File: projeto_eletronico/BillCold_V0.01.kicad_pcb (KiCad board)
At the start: 2 copper layers, 36 parts, among them J1 USB_B, U1 ESP32-S3, U2 AMS1117, U3 W25Q128JVSIQ, X1 OSCILADOR-3225

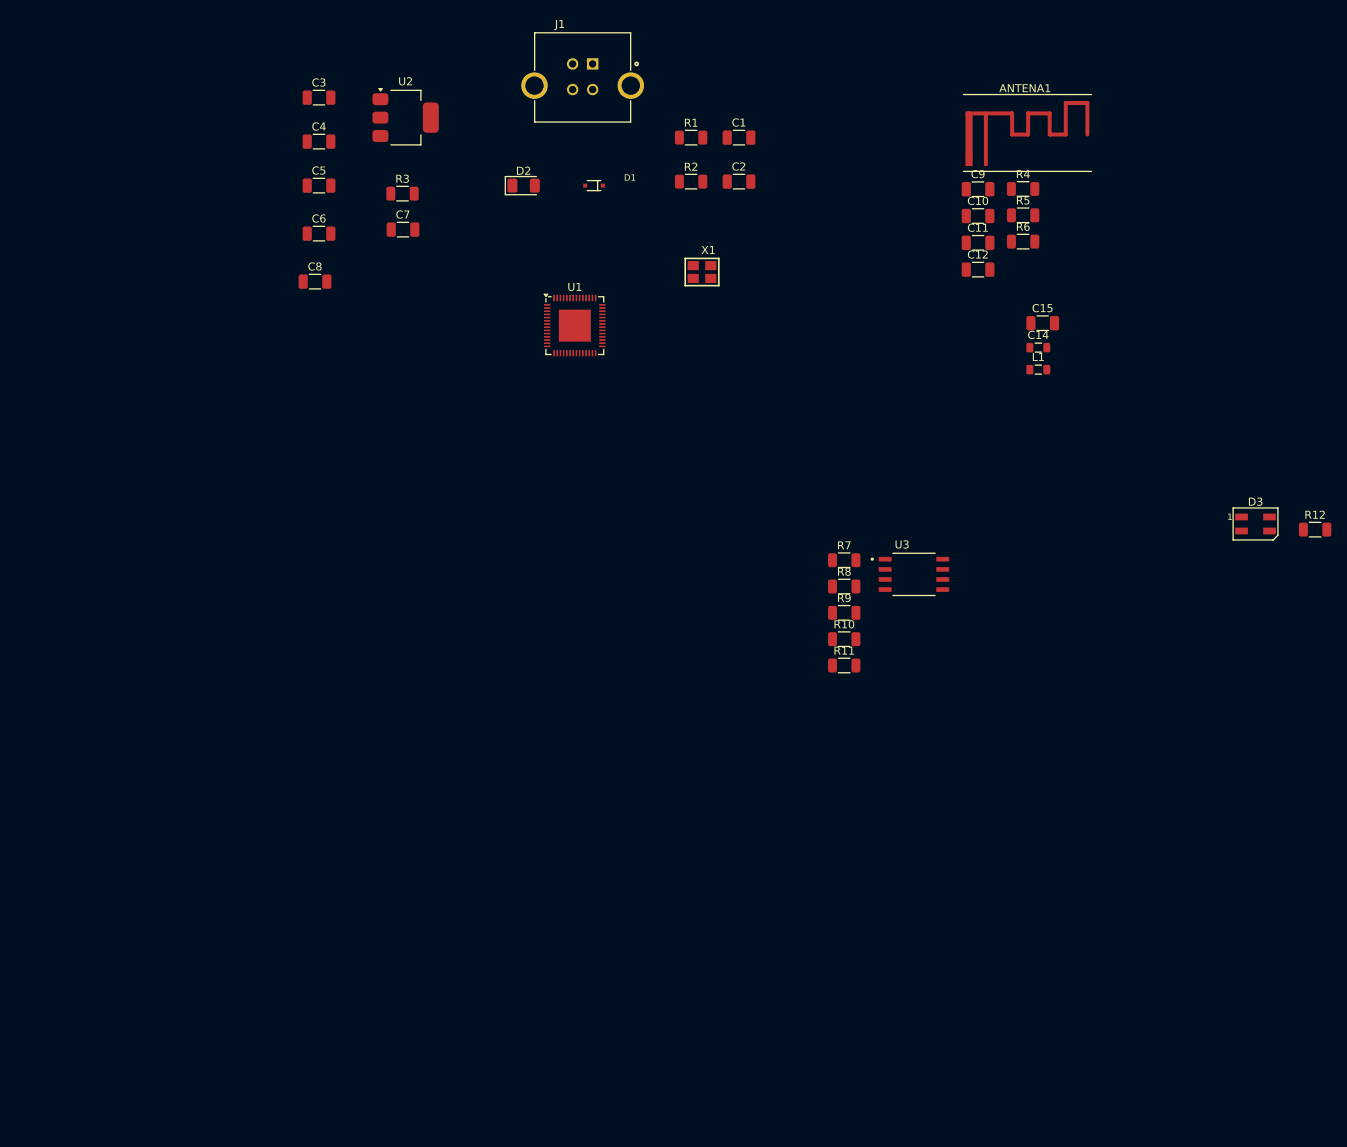
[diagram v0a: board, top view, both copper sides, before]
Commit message: Iniciando o roteamento das trilhas da PCB
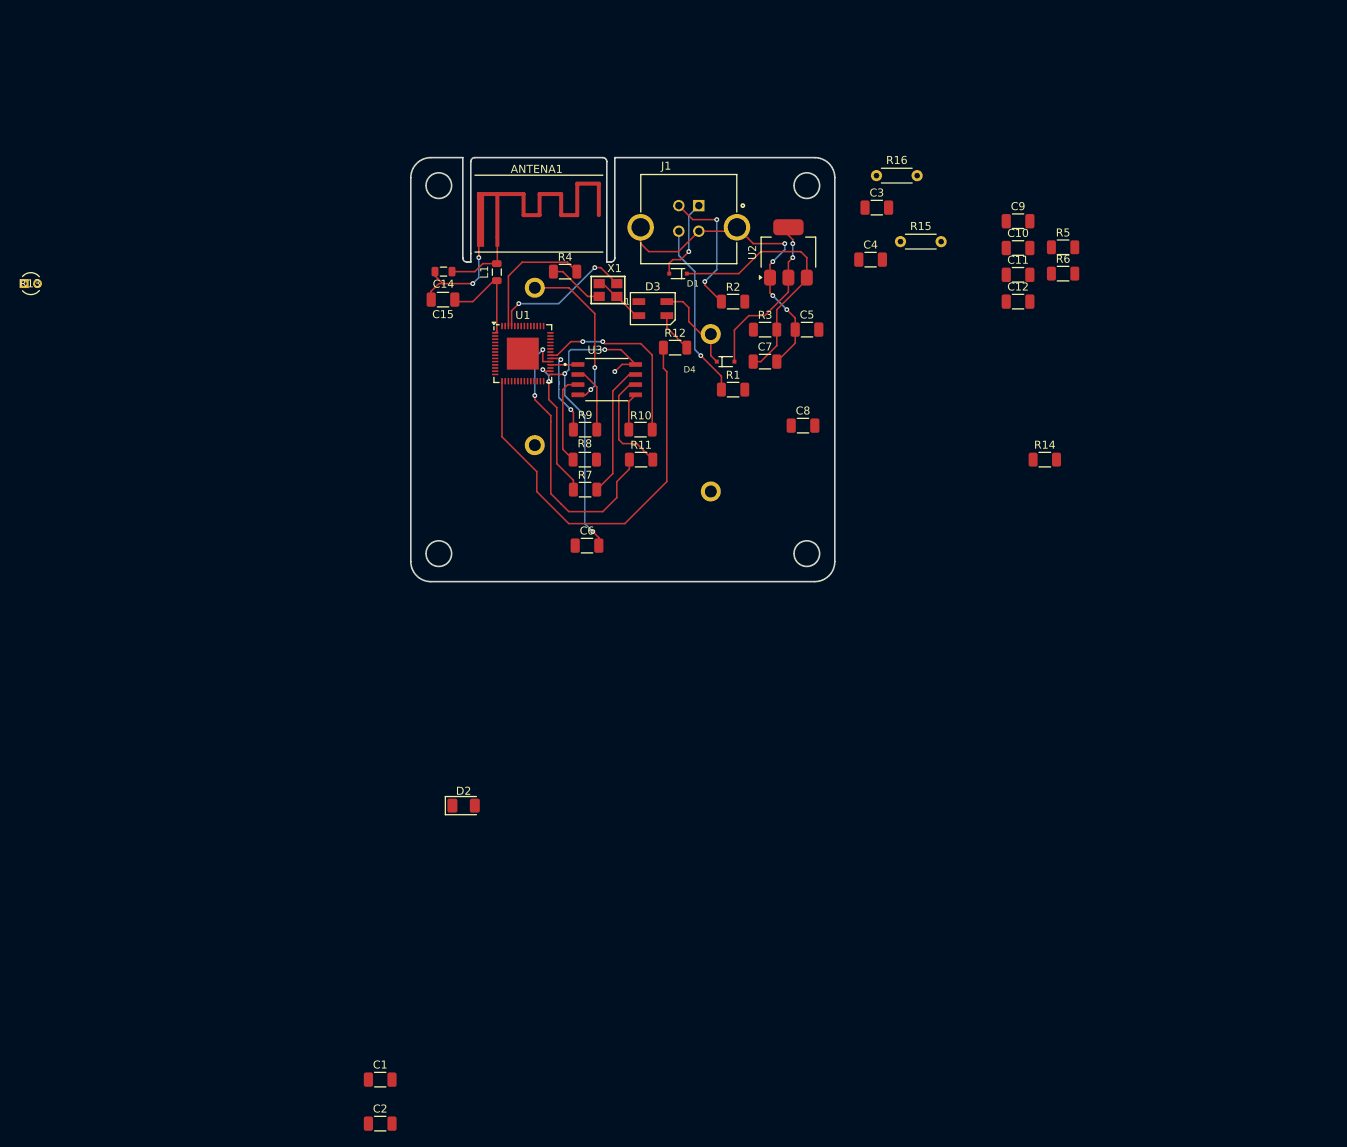
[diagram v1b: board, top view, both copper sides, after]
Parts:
- added CR1: ~, CR2450_SUPORT:CR2450_SUPORT, B.Cu at (151.0, 96.0)
- added CR2: ~, CR2450_SUPORT:CR2450_SUPORT, B.Cu at (173.0, 114.0)
- added D4: BAT760, BAT_760:SOD323_F_, F.Cu at (174.8, 101.5)
- added R13: MF11-502, MF11:TRES_MF52-A_CTM, F.Cu at (88.0, 91.8)
- added R14: 10K, Resistor_SMD:R_1206_3216Metric, F.Cu at (214.8, 113.8)
- added R15: 0, Resistor_THT:R_Axial_DIN0204_L3.6mm_D1.6mm_P5.08mm_Horizontal, F.Cu at (196.7, 86.5)
- added R16: 0, Resistor_THT:R_Axial_DIN0204_L3.6mm_D1.6mm_P5.08mm_Horizontal, F.Cu at (193.7, 78.2)
- moved C1 126.0 mm to (131.7, 191.2)
- moved C2 126.0 mm to (131.7, 196.8)
- moved R12 83.2 mm to (168.5, 99.8)
- moved D3 80.0 mm to (165.8, 94.9)
- moved D2 77.9 mm to (142.1, 157.0)
- moved C15 75.0 mm to (139.5, 93.8), turned to 180 degrees
- moved C14 75.0 mm to (139.6, 90.2), turned to 180 degrees
- moved C3 71.1 mm to (193.8, 82.2)
- moved C4 70.5 mm to (193.0, 88.8)
- moved L1 68.8 mm to (146.2, 90.3), turned to 90 degrees
- moved C5 63.6 mm to (185.0, 97.5)
- moved C8 63.6 mm to (184.5, 109.5)
- moved ANTENA1 61.9 mm to (148.8, 79.2)
- moved R4 58.2 mm to (154.8, 90.2)
- moved C6 51.4 mm to (157.5, 124.5)
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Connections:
- C8 pad 1: /VDD33 -> Net-(U2-VO)
- U1 pad 6: unconnected-(U1-GPIO1-Pad6) -> /GPIO1
- U1 pad 7: unconnected-(U1-GPIO2-Pad7) -> /GPIO2
- U2 pad 2: /VDD33 -> Net-(U2-VO)
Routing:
- net GND: track 0.00 -> 81.7 mm, vias 0 -> 8
- net /DATA_LED: track 0.00 -> 52.6 mm
- net /VDD_SPI: track 0.00 -> 40.3 mm, vias 0 -> 4
- net /SPICLK: track 0.00 -> 37.0 mm, vias 0 -> 2
- net /VIN_5V: track 0.00 -> 32.8 mm
- net /SPID: track 0.00 -> 23.4 mm, vias 0 -> 2
- net Net-(J1-D+): track 0.00 -> 22.0 mm, vias 0 -> 1
- net Net-(U2-VO): track 0.00 -> 21.2 mm, vias 0 -> 2
- net /XTAL_N: track 0.00 -> 18.1 mm, vias 0 -> 2
- net /SPIHD: track 0.00 -> 17.6 mm, vias 0 -> 2
- net Net-(J1-D-): track 0.00 -> 17.2 mm, vias 0 -> 2
- net Net-(U3-/HOLD/RESET(IO3)): track 0.00 -> 16.9 mm
- net /XTAL_P: track 0.00 -> 16.0 mm
- net Net-(U3-CLK): track 0.00 -> 13.5 mm
- net /LNA_IN: track 0.00 -> 13.0 mm
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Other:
- board outline added: 53 x 53 mm

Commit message: Projeto finalizado
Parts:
- added G***: LOGO, Logomarca:Termokip_V01, F.Cu at (174.5, 125.5)
- added LV-01: LOGO, Logomarca:Billhard_V01, F.Cu at (171.5, 122.2)
- added LV-01: LOGO, Logomarca:Billhard_V01, B.Cu at (151.5, 79.0)
- added REF**: WEEE-Logo_4.2x6mm_SilkScreen, Symbol:WEEE-Logo_4.2x6mm_SilkScreen, F.Cu at (185.5, 111.0)
- added REF**: ESD-Logo_6.6x6mm_SilkScreen, Symbol:ESD-Logo_6.6x6mm_SilkScreen, F.Cu at (180.5, 117.2)
- moved C2 100.8 mm to (180.8, 108.7)
- moved C1 99.2 mm to (180.8, 105.0)
- moved R5 78.1 mm to (139.5, 97.2), turned to 180 degrees
- moved R6 74.4 mm to (145.0, 109.0), turned to -90 degrees
- moved R14 72.1 mm to (143.0, 121.5), turned to 180 degrees
- moved C11 69.6 mm to (149.0, 121.5)
- moved R15 67.6 mm to (138.0, 120.0), turned to 90 degrees
- moved R13 65.7 mm to (144.2, 125.8)
- moved R16 62.6 mm to (138.0, 106.8), turned to -90 degrees
- moved D2 59.2 mm to (170.3, 105.0)
- moved C9 54.5 mm to (158.5, 97.0)
- moved C12 43.3 mm to (173.0, 114.0)
- moved C3 36.3 mm to (171.0, 110.5)
- moved C10 32.2 mm to (180.0, 80.0)
- moved C4 27.6 mm to (176.0, 110.5), turned to 180 degrees
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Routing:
- net /VDD33: track 12.0 -> 143.5 mm, vias 0 -> 10
- net GND: track 81.7 -> 201.0 mm
- net /D-: track 0.00 -> 44.1 mm, vias 0 -> 4
- net /VDD_SPI: track 40.3 -> 72.2 mm, vias 4 -> 5
- net /D+: track 0.00 -> 31.8 mm, vias 0 -> 4
- net /GPIO2: track 0.00 -> 31.4 mm
- net /XTAL_N: track 18.1 -> 46.1 mm
- net Net-(R13-Pad2): track 0.00 -> 24.8 mm, vias 0 -> 3
- net /M_TXD0: track 0.00 -> 22.1 mm, vias 0 -> 2
- net Net-(J1-D-): track 17.2 -> 37.0 mm
- net /GPIO1: track 0.00 -> 19.0 mm
- net /SPIWP: track 0.00 -> 18.4 mm, vias 0 -> 2
- net /GPIO45: track 0.00 -> 17.1 mm, vias 0 -> 2
- net Net-(D2-A): track 0.00 -> 14.3 mm, vias 0 -> 2
- net Net-(U2-VO): track 21.2 -> 31.9 mm, vias 2 -> 4
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- added copper zone on B.Cu, net GND
- added copper zone on F.Cu, net GND
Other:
- board text added: "Versão do hardware: 1.0"

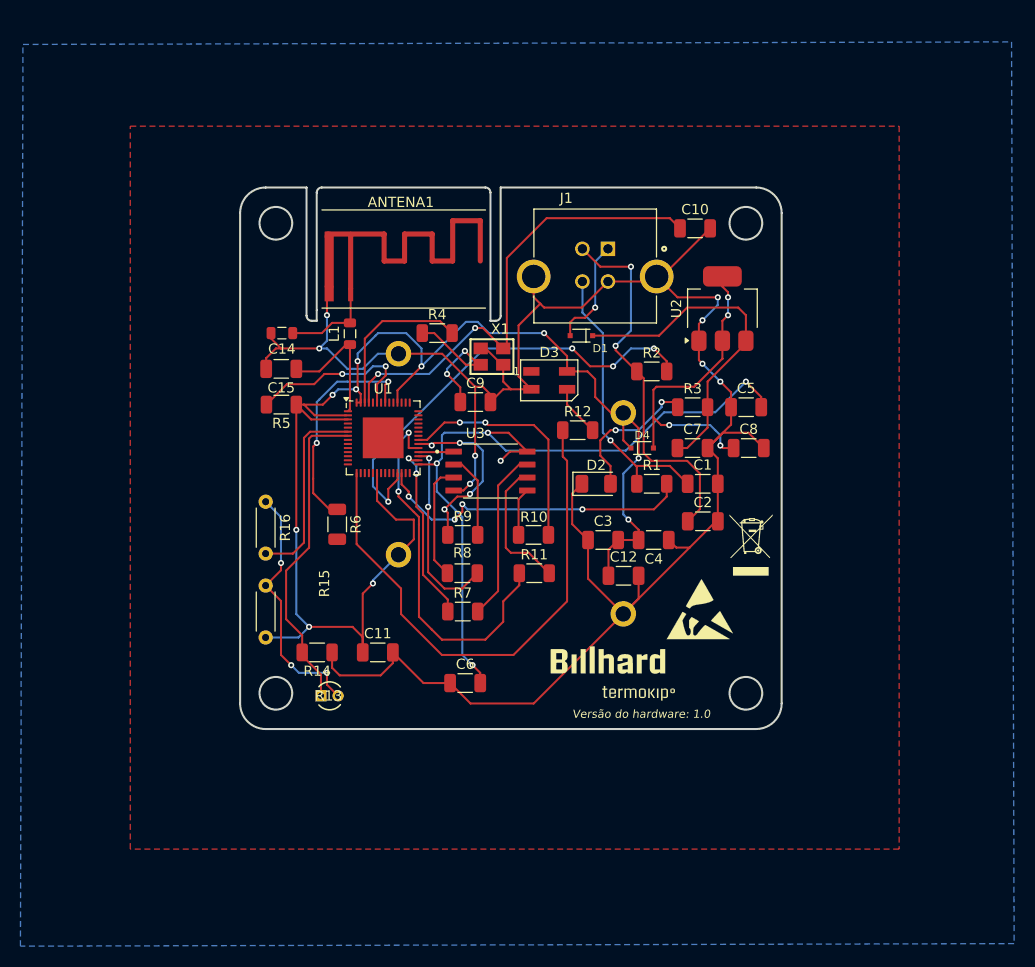
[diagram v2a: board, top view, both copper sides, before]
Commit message: Alterando componentes smd 0603
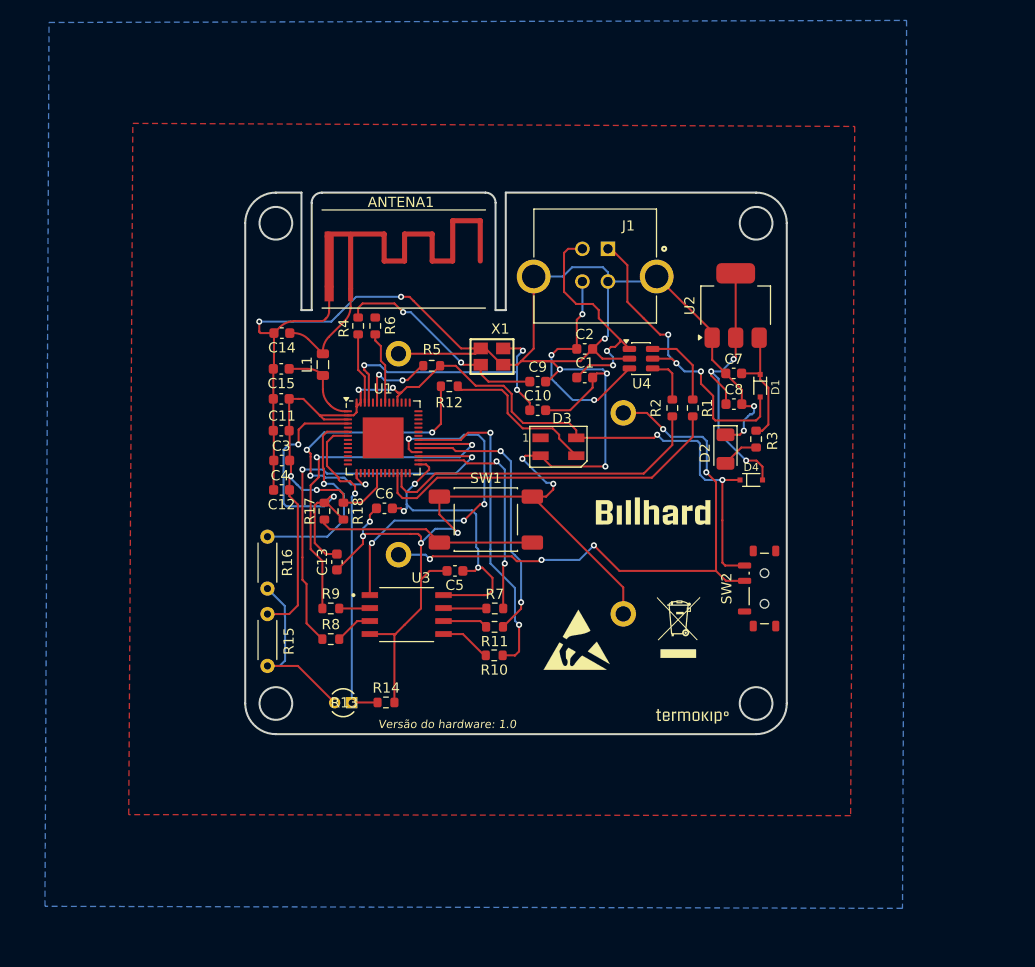
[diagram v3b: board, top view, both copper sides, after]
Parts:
- added C13: 100nF, Capacitor_SMD:C_0603_1608Metric, F.Cu at (145.0, 112.7)
- added R17: 0, Resistor_SMD:R_0603_1608Metric, F.Cu at (143.8, 107.7)
- added R18: 10K, Resistor_SMD:R_0603_1608Metric, F.Cu at (145.6, 107.7)
- added SW1: SW_Push, Button_Switch_SMD:SW_Push_1P1T_NO_E-Switch_TL3301NxxxxxG, F.Cu at (159.6, 108.5)
- added SW2: SW_SPDT_321, Button_Switch_SMD:SW_SPDT_Shouhan_MSK12C02, F.Cu at (186.8, 115.2)
- added U4: USBLC6-2SC6, Package_TO_SOT_SMD:SOT-23-6, F.Cu at (174.7, 92.8)
- C1, C2: value C -> 1pF; footprint Capacitor_SMD:C_1206_3216Metric -> Capacitor_SMD:C_0603_1608Metric
- C10, C9: value 15pF -> 18pF; footprint Capacitor_SMD:C_1206_3216Metric -> Capacitor_SMD:C_0603_1608Metric
- C11, C12, C15, C3, C4, C5, C6, C7, C8: footprint Capacitor_SMD:C_1206_3216Metric -> Capacitor_SMD:C_0603_1608Metric
- C14: footprint Inductor_SMD:L_0805_2012Metric -> Capacitor_SMD:C_0603_1608Metric
- R1, R10, R11, R12, R14, R2, R3, R4, R5, R6, R7, R8, R9: footprint Resistor_SMD:R_1206_3216Metric -> Resistor_SMD:R_0603_1608Metric
- moved C4 37.2 mm to (139.6, 102.7), turned to 0 degrees
- moved C12 34.5 mm to (139.6, 105.6), turned to 180 degrees
- moved C3 33.3 mm to (139.5, 99.8)
- moved C5 32.7 mm to (156.5, 113.5)
- moved C11 26.6 mm to (139.5, 96.7), turned to 180 degrees
- moved C10 23.5 mm to (164.6, 97.8)
- moved C2 20.4 mm to (169.2, 91.8)
- moved R6 19.8 mm to (148.7, 89.5), turned to 90 degrees
- moved C6 18.8 mm to (149.6, 107.4)
- moved D1 18.2 mm to (186.4, 95.4), turned to 90 degrees
- moved U3 16.3 mm to (151.8, 117.8)
- moved C1 15.5 mm to (169.2, 94.6)
- moved LV-01 15.2 mm to (175.9, 107.7)
- moved R5 15.2 mm to (154.2, 93.5)
- moved R9 14.8 mm to (144.4, 117.2)
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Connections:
- C1 pad 1: Net-(J1-D+) -> /D_N
- C2 pad 1: Net-(J1-D-) -> /D_P
- CR1 pad 2: /VDD33 -> /VDD_BAT
- CR2 pad 2: /VDD33 -> /VDD_BAT
- J1 pad 2: Net-(J1-D-) -> /D_N
- J1 pad 3: Net-(J1-D+) -> /D_P
- R1 pad 1: Net-(J1-D+) -> Net-(R1-Pad1)
- R1 pad 2: /D+ -> /D-
- R2 pad 1: Net-(J1-D-) -> Net-(R2-Pad1)
- R2 pad 2: /D- -> /D+
- U1 pad 4: unconnected-(U1-CHIP_PU-Pad4) -> /EN
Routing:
- net /VDD_BAT: track 0.00 -> 58.9 mm, vias 0 -> 5
- net /VDD_SPI: track 72.2 -> 29.9 mm, vias 5 -> 3
- net GND: track 201.0 -> 238.9 mm, vias 8 -> 14
- net Net-(J1-D-): track 37.0 -> 0.00 mm, vias 2 -> 0
- net /VDD33: track 143.5 -> 107.6 mm, vias 10 -> 6
- net /SPICS0: track 3.47 -> 33.8 mm, vias 0 -> 4
- net /EN: track 0.00 -> 30.0 mm, vias 0 -> 2
- net Net-(J1-D+): track 27.8 -> 0.00 mm, vias 1 -> 0
- net /DATA_LED: track 52.6 -> 28.0 mm, vias 0 -> 4
- net /D_N: track 0.00 -> 22.5 mm, vias 0 -> 2
- net /SPIWP: track 18.4 -> 40.1 mm
- net /D_P: track 0.00 -> 21.6 mm, vias 0 -> 3
- net Net-(R17-Pad1): track 0.00 -> 21.5 mm
- net Net-(J1-VBUS): track 10.6 -> 31.7 mm, vias 1 -> 3
- net /VIN_5V: track 32.8 -> 12.2 mm
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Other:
- outline, holes or cut-outs redrawn

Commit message: Conclusão do projeto
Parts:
- removed ANTENA1: ANT_2.4GB, ANTENA_2.4GZ:Antena_2.4GB
- removed D3: SK6812MINI, LED_SMD:LED_SK6812MINI_PLCC4_3.5x3.5mm_P1.75mm
- removed the REF** at (178.4, 119.0)
- added AE1: Antenna_Shield, RF_Antenna:Texas_SWRA117D_2.4GHz_Right, F.Cu at (146.9, 84.2)
- added C16: 10u, Capacitor_SMD:C_0603_1608Metric, F.Cu at (150.9, 90.2)
- added C17: 1u, Capacitor_SMD:C_0603_1608Metric, F.Cu at (154.0, 90.2)
- added C18: 100n, Capacitor_SMD:C_0603_1608Metric, F.Cu at (157.1, 90.2)
- added C19: 100n, Capacitor_SMD:C_0603_1608Metric, F.Cu at (160.4, 90.2)
- added C20: 100n, Capacitor_SMD:C_0603_1608Metric, F.Cu at (138.3, 123.2)
- added C21: 100n, Capacitor_SMD:C_0603_1608Metric, F.Cu at (167.4, 98.2)
- added C22: 4.7u, Capacitor_SMD:C_0603_1608Metric, F.Cu at (165.3, 98.2)
- added D5: SK6812, LED_SMD:LED_WS2812B-Mini_PLCC4_3.5x3.5mm, F.Cu at (146.7, 116.8)
- added F2: 600Ω, Inductor_SMD:L_0805_2012Metric, F.Cu at (144.6, 95.9)
- added J2: Screw_Terminal_01x08, TerminalBlock:TerminalBlock_MaiXu_MX126-5.0-08P_1x08_P5.00mm, F.Cu at (145.1, 124.5)
- added R19: 10k, Resistor_SMD:R_0603_1608Metric, F.Cu at (139.1, 86.4)
- added R20: 470, Resistor_SMD:R_0603_1608Metric, F.Cu at (183.4, 111.7)
- added R21: 10K, Resistor_SMD:R_0603_1608Metric, F.Cu at (139.1, 83.6)
- added SW3: SW_Push, Button_Switch_SMD:SW_Push_1P1T_NO_E-Switch_TL3301NxxxxxG, F.Cu at (181.8, 116.2)
- added SW4: SW_Reed, Resistor_THT:R_Axial_DIN0614_L14.3mm_D5.7mm_P20.32mm_Horizontal, F.Cu at (139.6, 110.3)
- C1, C2: value 1pF -> NC
- C11: value 0.1uF -> 1.1uF
- C12: value 0.1uF -> 100nF
- C3: value 10uF -> 1u
- C4: value 1uF -> 100nF
- C5: value 0.1uF -> 100n
- R1, R2: value 0h -> 0Ω
- R10, R11, R17, R4, R7, R8, R9: value 0 -> 0Ω
- R12: value 0 -> 360
- R6: value 499 -> 33
- moved R16 52.7 mm to (187.3, 96.3), turned to 180 degrees
- moved R15 47.4 mm to (182.2, 100.2), turned to 0 degrees
- moved C12 37.9 mm to (177.3, 102.1)
- moved R6 30.5 mm to (177.3, 100.5), turned to 0 degrees
- moved G*** 30.2 mm to (177.5, 97.6)
- moved R17 30.0 mm to (173.8, 108.7), turned to 180 degrees
- moved U4 27.8 mm to (154.8, 112.2), turned to 180 degrees
- moved REF** 26.3 mm to (146.0, 106.6)
- moved R9 25.9 mm to (162.2, 98.3), turned to -90 degrees
- moved R18 24.9 mm to (170.5, 108.7), turned to 0 degrees
- moved C6 23.7 mm to (172.3, 100.4), turned to 180 degrees
- moved C13 22.4 mm to (167.0, 108.7), turned to 180 degrees
- moved D2 22.3 mm to (182.4, 79.3)
- moved C11 22.0 mm to (159.2, 86.8), turned to 90 degrees
- moved R8 19.5 mm to (160.6, 109.3), turned to 90 degrees
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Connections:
- C1 pad 1: /D_N -> Net-(C1-Pad1)
- C2 pad 1: /D_P -> Net-(C2-Pad1)
- J1 pad 2: /D_N -> Net-(J1-D-)
- J1 pad 3: /D_P -> Net-(J1-D+)
- R1 pad 1: Net-(R1-Pad1) -> Net-(C1-Pad1)
- R1 pad 2: /D- -> Net-(J1-D-)
- R2 pad 1: Net-(R2-Pad1) -> Net-(J1-D+)
- R2 pad 2: /D+ -> Net-(C2-Pad1)
- U1 pad 10: unconnected-(U1-GPIO5-Pad10) -> /GPIO5
- U1 pad 15: /DATA_LED -> unconnected-(U1-GPIO10-Pad15)
- U1 pad 2: /VDD33 -> /VDD3P3
- U1 pad 23: unconnected-(U1-GPIO17-Pad23) -> /TX_LORA
- U1 pad 24: unconnected-(U1-GPIO18-Pad24) -> /RX_LORA
- U1 pad 27: unconnected-(U1-GPIO21-Pad27) -> /AU_LORA
- U1 pad 3: /VDD33 -> /VDD3P3
- U1 pad 38: unconnected-(U1-GPIO33-Pad38) -> /M0_LORA
- U1 pad 39: unconnected-(U1-GPIO34-Pad39) -> /M1_LORA
- U1 pad 5: unconnected-(U1-GPIO0-Pad5) -> /BOOT
- U1 pad 57: unconnected-(U1-GND-Pad57) -> GND
- U1 pad 9: unconnected-(U1-GPIO4-Pad9) -> /DATA_LED
- U4 pad 1: /D_N -> Net-(C2-Pad1)
- U4 pad 3: /D_P -> Net-(C1-Pad1)
- U4 pad 4: Net-(R2-Pad1) -> /D-
- U4 pad 6: Net-(R1-Pad1) -> /D+
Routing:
- net /BOOT: track 0.00 -> 109.8 mm, vias 0 -> 6
- net /VIN_5V: track 12.2 -> 121.0 mm, vias 0 -> 3
- net /VDD33: track 107.6 -> 199.8 mm, vias 6 -> 17
- net GND: track 238.9 -> 327.3 mm, vias 14 -> 12
- net Net-(R13-Pad2): track 17.8 -> 87.8 mm
- net Net-(C2-Pad1): track 0.00 -> 60.3 mm, vias 0 -> 2
- net Net-(J1-VBUS): track 31.7 -> 81.6 mm, vias 3 -> 9
- net /GPIO1: track 20.4 -> 69.5 mm, vias 1 -> 0
- net Net-(C1-Pad1): track 0.00 -> 48.2 mm, vias 0 -> 2
- net /AU_LORA: track 0.00 -> 47.1 mm, vias 0 -> 3
- net /M1_LORA: track 0.00 -> 43.8 mm, vias 0 -> 3
- net /M0_LORA: track 0.00 -> 39.0 mm, vias 0 -> 1
- net /GPIO5: track 0.00 -> 33.5 mm, vias 0 -> 4
- net /RX_LORA: track 0.00 -> 29.0 mm, vias 0 -> 3
- net /TX_LORA: track 0.00 -> 28.0 mm, vias 0 -> 2
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- added copper zone on B.Cu, net (none)
- added copper zone on F.Cu, net (none)
- removed copper zone on B.Cu, net GND
- removed copper zone on F.Cu, net GND
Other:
- board text added: "3.3V"
- board text added: "5V"
- board text added: "Boot"
- board text added: "GND"
- board text added: "IO17"
- board text added: "IO18"
- board text added: "IO21"
- board text added: "IO33"
- board text added: "IO34"
- board text added: "Reset"
- board text added: "V: 0.1"
- board text removed: "Versão do hardware: 1.0"
